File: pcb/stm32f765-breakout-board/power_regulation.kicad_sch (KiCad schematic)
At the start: 16 parts, among them U2 AMS1117-3.3

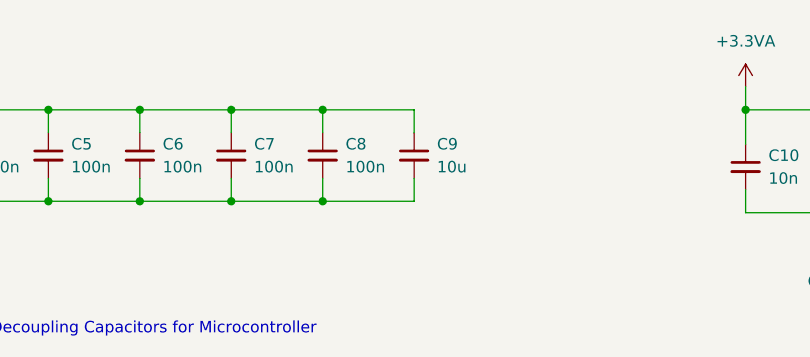
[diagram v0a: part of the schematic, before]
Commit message: added lsm6dsl to pcb and ordered v3
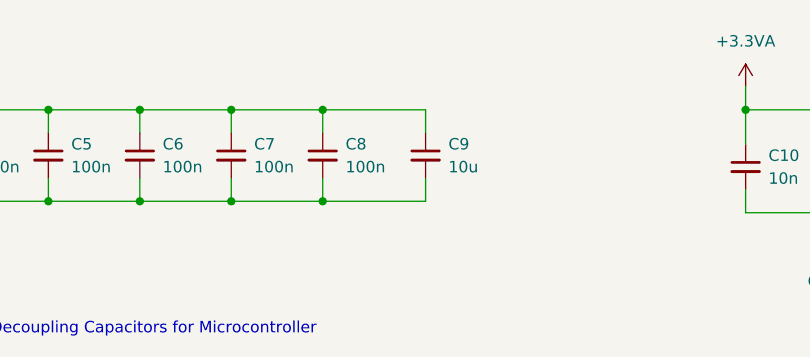
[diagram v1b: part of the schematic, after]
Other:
- moved on the sheet: C9
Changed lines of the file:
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@@
 	(wire
 		(pts
-			(xy 81.28 104.14) (xy 91.44 104.14)
+			(xy 81.28 104.14) (xy 92.71 104.14)
 		)
 		(stroke
@@
 	(wire
 		(pts
-			(xy 81.28 93.98) (xy 91.44 93.98)
+			(xy 81.28 93.98) (xy 92.71 93.98)
 		)
 		(stroke
@@
 	(wire
 		(pts
-			(xy 91.44 93.98) (xy 91.44 96.52)
+			(xy 92.71 93.98) (xy 92.71 96.52)
 		)
 		(stroke
@@
 	(wire
 		(pts
-			(xy 91.44 104.14) (xy 91.44 101.6)
+			(xy 92.71 104.14) (xy 92.71 101.6)
 		)
 		(stroke
@@
 		(polyline
 			(pts
-				(xy 22.86 81.28) (xy 99.06 81.28) (xy 99.06 123.19) (xy 22.86 123.19)
+				(xy 22.86 81.28) (xy 110.998 81.153) (xy 110.998 123.063) (xy 22.86 123.19)
 			)
 			(stroke
@@
 	(symbol
 		(lib_id "Device:C_Small")
-		(at 91.44 99.06 0)
+		(at 92.71 99.06 0)
 		(unit 1)
 		(exclude_from_sim no)
@@
 		(fields_autoplaced yes)
 		(property "Reference" "C9"
-			(at 93.98 97.7962 0)
+			(at 95.25 97.7962 0)
 			(effects
 				(font
@@
 		)
 		(property "Value" "10u"
-			(at 93.98 100.3362 0)
+			(at 95.25 100.3362 0)
 			(effects
 				(font
@@
 		)
 		(property "Footprint" "Capacitor_SMD:C_0805_2012Metric_Pad1.18x1.45mm_HandSolder"
-			(at 91.44 99.06 0)
+			(at 92.71 99.06 0)
 			(effects
 				(font
@@
 		)
 		(property "Datasheet" "~"
-			(at 91.44 99.06 0)
+			(at 92.71 99.06 0)
 			(effects
 				(font
@@
 		)
 		(property "Description" "Unpolarized capacitor, small symbol"
-			(at 91.44 99.06 0)
+			(at 92.71 99.06 0)
 			(effects
 				(font
@@
 		)
 		(property "Robu SKU" "1544904"
-			(at 91.44 99.06 0)
+			(at 92.71 99.06 0)
 			(effects
 				(font
@@
 		)
 		(property "KLC_S3.3" ""
-			(at 91.44 99.06 0)
+			(at 92.71 99.06 0)
 			(effects
 				(font
@@
 		)
 		(property "KLC_S4.1" ""
-			(at 91.44 99.06 0)
-			(effects
-				(font
+			(at 92.71 99.06 0)
+			(effects
+				(font

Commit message: Updated titleblock on f765 breakout pcb
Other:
- company: (none) -> Pranav Chandra N. V.
- title: (none) -> STM32F765VIT6 Breakout Board
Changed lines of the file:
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@@
 	(generator_version "9.0")
 	(paper "A4")
+	(title_block
+		(title "STM32F765VIT6 Breakout Board")
+		(date "2026-04-17")
+		(rev "v5")
+		(company "Pranav Chandra N. V.")
+		(comment 1 "v4: Updated analog circuitry filtering")
+	)
 	(text "Filtering for 3.3VA"
 		(exclude_from_sim no)

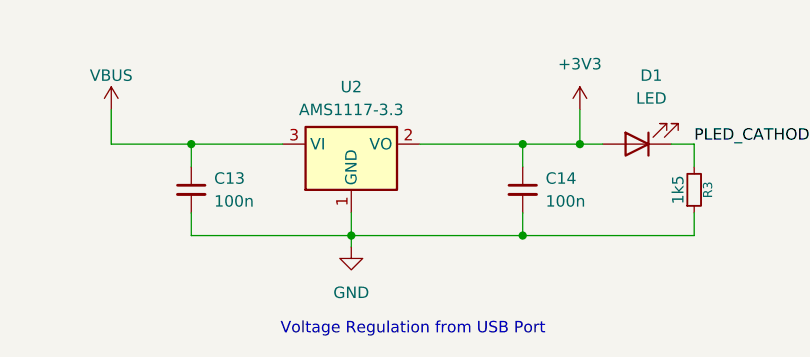
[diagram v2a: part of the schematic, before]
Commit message: Added on board LED to PCB and blinky for board
v6 of the PCB now has an in built on board LED to PE02, to allow for
faster debugging.

The first assembled prototype finally worked, and a blinky sketch was
flashed to test. Relevant code has been added to firmware.
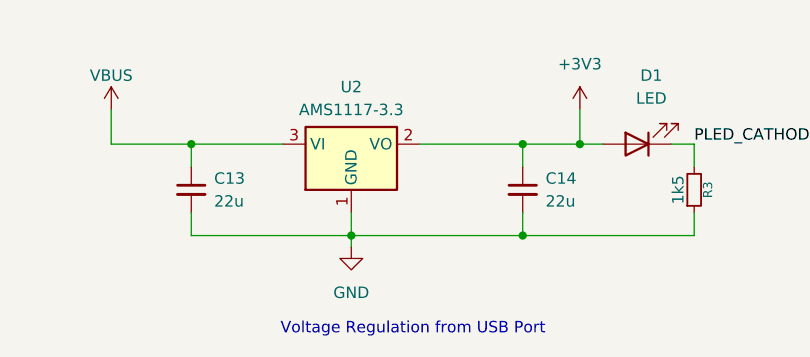
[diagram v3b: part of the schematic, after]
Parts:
- C13, C14: value 100n -> 22u
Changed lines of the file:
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@@
 		(company "Pranav Chandra N. V.")
 		(comment 1 "v4: Updated analog circuitry filtering")
+		(comment 2 "v5: Changed 3V3 filtering capacitance to the correct amount")
 	)
 	(text "Filtering for 3.3VA"
@@
 				)
 			)
+			(project "power_regulation"
+				(path "/f2a20289-2ff4-41ff-b7e9-ec9f4af5d676"
+					(reference "C?")
+					(unit 1)
+				)
+			)
 		)
 	)
@@
 				)
 			)
+			(project "power_regulation"
+				(path "/f2a20289-2ff4-41ff-b7e9-ec9f4af5d676"
+					(reference "C?")
+					(unit 1)
+				)
+			)
 		)
 	)
@@
 				)
 			)
+			(project "power_regulation"
+				(path "/f2a20289-2ff4-41ff-b7e9-ec9f4af5d676"
+					(reference "#PWR?")
+					(unit 1)
+				)
+			)
 		)
 	)
@@
 				)
 			)
+			(project "power_regulation"
+				(path "/f2a20289-2ff4-41ff-b7e9-ec9f4af5d676"
+					(reference "C?")
+					(unit 1)
+				)
+			)
 		)
 	)
@@
 				)
 			)
+			(project "power_regulation"
+				(path "/f2a20289-2ff4-41ff-b7e9-ec9f4af5d676"
+					(reference "#PWR?")
+					(unit 1)
+				)
+			)
 		)
 	)
@@
 				)
 			)
+			(project "power_regulation"
+				(path "/f2a20289-2ff4-41ff-b7e9-ec9f4af5d676"
+					(reference "C?")
+					(unit 1)
+				)
+			)
 		)
 	)
@@
 				)
 			)
+			(project "power_regulation"
+				(path "/f2a20289-2ff4-41ff-b7e9-ec9f4af5d676"
+					(reference "#PWR?")
+					(unit 1)
+				)
+			)
 		)
 	)
@@
 			)
 		)
-		(property "Value" "100n"
+		(property "Value" "22u"
 			(at 242.57 104.1462 0)
 			(effects
@@
 				(path "/256bcd66-93a7-4ec7-b605-dbc945027d42/237a83a1-cd93-40bd-95c3-484e4b737075"
 					(reference "C14")
+					(unit 1)
+				)
+			)
+			(project "power_regulation"
+				(path "/f2a20289-2ff4-41ff-b7e9-ec9f4af5d676"
+					(reference "C?")
 					(unit 1)
 				)
@@
 				)
 			)
+			(project "power_regulation"
+				(path "/f2a20289-2ff4-41ff-b7e9-ec9f4af5d676"
+					(reference "R?")
+					(unit 1)
+				)
+			)
 		)
 	)
@@
 				)
 			)
+			(project "power_regulation"
+				(path "/f2a20289-2ff4-41ff-b7e9-ec9f4af5d676"
+					(reference "#PWR?")
+					(unit 1)
+				)
+			)
 		)
 	)
@@
 				)
 			)
+			(project "power_regulation"
+				(path "/f2a20289-2ff4-41ff-b7e9-ec9f4af5d676"
+					(reference "C?")
+					(unit 1)
+				)
+			)
 		)
 	)
@@
 				)
 			)
+			(project "power_regulation"
+				(path "/f2a20289-2ff4-41ff-b7e9-ec9f4af5d676"
+					(reference "C?")
+					(unit 1)
+				)
+			)
 		)
 	)
@@
 				)
 			)
+			(project "power_regulation"
+				(path "/f2a20289-2ff4-41ff-b7e9-ec9f4af5d676"
+					(reference "FB?")
+					(unit 1)
+				)
+			)
 		)
 	)
@@
 				)
 			)
+			(project "power_regulation"
+				(path "/f2a20289-2ff4-41ff-b7e9-ec9f4af5d676"
+					(reference "U?")
+					(unit 1)
+				)
+			)
 		)
 	)
@@
 				)
 			)
+			(project "power_regulation"
+				(path "/f2a20289-2ff4-41ff-b7e9-ec9f4af5d676"
+					(reference "C?")
+					(unit 1)
+				)
+			)
 		)
 	)
@@
 				)
 			)
+			(project "power_regulation"
+				(path "/f2a20289-2ff4-41ff-b7e9-ec9f4af5d676"
+					(reference "#PWR?")
+					(unit 1)
+				)
+			)
 		)
 	)
@@
 				)
 			)
+			(project "power_regulation"
+				(path "/f2a20289-2ff4-41ff-b7e9-ec9f4af5d676"
+					(reference "C?")
+					(unit 1)
+				)
+			)
 		)
 	)
@@
 				)
 			)
+			(project "power_regulation"
+				(path "/f2a20289-2ff4-41ff-b7e9-ec9f4af5d676"
+					(reference "#PWR?")
+					(unit 1)
+				)
+			)
 		)
 	)
@@
 				(path "/256bcd66-93a7-4ec7-b605-dbc945027d42/237a83a1-cd93-40bd-95c3-484e4b737075"
 					(reference "#PWR015")
+					(unit 1)
+				)
+			)
+			(project "power_regulation"
+				(path "/f2a20289-2ff4-41ff-b7e9-ec9f4af5d676"
+					(reference "#PWR?")
 					(unit 1)
 				)
@@
 				)
 			)
+			(project "power_regulation"
+				(path "/f2a20289-2ff4-41ff-b7e9-ec9f4af5d676"
+					(reference "#PWR?")
+					(unit 1)
+				)
+			)
 		)
 	)
@@
 			)
 		)
-		(property "Value" "100n"
+		(property "Value" "22u"
 			(at 205.74 104.1462 0)
 			(effects
@@
 				(path "/256bcd66-93a7-4ec7-b605-dbc945027d42/237a83a1-cd93-40bd-95c3-484e4b737075"
 					(reference "C13")
+					(unit 1)
+				)
+			)
+			(project "power_regulation"
+				(path "/f2a20289-2ff4-41ff-b7e9-ec9f4af5d676"
+					(reference "C?")
 					(unit 1)
 				)
@@
 				)
 			)
+			(project "power_regulation"
+				(path "/f2a20289-2ff4-41ff-b7e9-ec9f4af5d676"
+					(reference "C?")
+					(unit 1)
+				)
+			)
 		)
 	)
@@
 				)
 			)
+			(project "power_regulation"
+				(path "/f2a20289-2ff4-41ff-b7e9-ec9f4af5d676"
+					(reference "#PWR?")
+					(unit 1)
+				)
+			)
 		)
 	)
@@
 				)
 			)
+			(project "power_regulation"
+				(path "/f2a20289-2ff4-41ff-b7e9-ec9f4af5d676"
+					(reference "C?")
+					(unit 1)
+				)
+			)
 		)
 	)
@@
 				)
 			)
-		)
-	)
+			(project "power_regulation"
+				(path "/f2a20289-2ff4-41ff-b7e9-ec9f4af5d676"
+					(reference "D?")
+					(unit 1)
+				)
+			)
+		)
+	)
+	(sheet_instances
+		(path "/"
+			(page "1")
+		)
+	)
+	(embedded_fonts no)
+	(embedded_files
+		(file
+			(name "main_template.kicad_wks")
+			(type worksheet)
+			(data |KLUv/WCHCq0VAKYeYSEA1TZqxSYpSnAbvBZXs5wAOGKZeWHW4zrjCpNZ+v8JBRNXAFAAWwCj/tcf
+				qX+jwXtSz1izvRHzmSsWLKWmbz7EoJuxWLAU9TvC5YfuEwCAAOn5W04KmzDT1o/DixHJybd+b998
+				NQRAoHBRSqs6q2eNy30/BECg7IAwoQfiDiGfdYa6rV5qcqKTf+j+93ZWtvq0otAGM37vknfvm7cG
+				X/Tpc+qAWvz8io/f7+Y9zB69PZ/88x1HDVbHLoyiHuZ7UdP6pNR/e19Ok9/Ryw/eHd64dcb3Jb0J
+				RZtkkxHmQlF/btXNolE+l3JdkzsoZTk2aUSycRTNgllkis1BGlgKow6OuEpaly0wWoXjNtLAE/e9
+				xd5btO/nC7oog7/0cGx1momq9fl936QVIBCBgnVRC3Ed5qRsddl6qBaramVVrKKHOivaRTSIKHvk
+				qBWzXiLZBCJRIBpdNuk0rcFdV0VZkCyiPTYGZoBY9B57oXpFUJNqj27rxMddpSH2v3fDCQwlQbhN
+				/gGAiaABSYYUDYkkSQoZ5oBEpOaoOozVNJ4pks/fiE0ZYQwgJSGD6wSyrriywopiggHII25zAoVs
+				XFbx0JeoRBjENn6ZPNfwMAiB7v1Jao+tsR3fbItsc6cfa22SwPMnbyvPHcsCfNiQbTqtxVlLMuyT
+				Q1CBRmZJpUc4pQ9d6hFpkGKo5kDuOq5adyoQnBVWLyX04o7iaQH+xWIuAKszPgbRT71kepu0ahHJ
+				5rySzSN2G6MZTKGEeFgCpeAjEDEylaH6xVARFuhl3ozP4iGJaeTxSXanUpT5cOL42wR3pphhO//Z
+				40AJWebRI0cgaGFkJ8ZBXrR3eNWHXAgAXP2GzD6THl2sihfFfNSB65xJb3veSYfQvsmqkQcUuzti
+				bryslIAVCnt4R7z3TYeQjY9eBQ==|
+			)
+			(checksum "2F156D714875550A13BB058F8E490E47")
+		)
+	)
